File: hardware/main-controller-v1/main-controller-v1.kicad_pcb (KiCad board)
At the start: 2 copper layers, 213.5 x 134.1 mm, 63 parts, among them J1 USB_C_Receptacle_USB2.0_16P, J2 Screw_Terminal_01x02, J3 Screw_Terminal_01x02, J4 Screw_Terminal_01x02, J6 Screw_Terminal_01x14, K1 G3MB-202P, K10 G3MB-202P, K11 G3MB-202P, K12 G3MB-202P, K2 G3MB-202P, K3 G3MB-202P, K4 G3MB-202P, K5 G3MB-202P, K6 G3MB-202P, K7 G3MB-202P, K8 G3MB-202P, K9 G3MB-202P, SW1 SW_Push, SW2 SW_Push, U1 ESP32-S3-WROOM-1, U2 USBLC6-2SC6, U3 LM2596S-5, U4 AP2112K-3.3

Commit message: feat(hardware): WP-24BF*15 PCB outline with parametric IR + KiCad renderer
Board outline for the smaller Polycase WP-24BF*15 enclosure, driven by a
JSON intermediate representation so future geometry tweaks stay in one place.

- board_ir.json: authoritative dimensions in inches, origin at board center.
  Includes concave R.300 corner scoops (to clear lid-screw bosses),
  case-rib alignment notches, 4 corner mounting holes, and a top-edge
  antenna cutout (20 mm x 8.75 mm) sized to clear the WROOM-1 antenna
  keep-out plus the same boss column that the standard case-rib notches
  address.
- preview_outline.py: matplotlib preview emitting the same segment list
  the KiCad renderer consumes, with a closure check so gaps are caught
  before touching the .pcb.
- draw_24f_outline.py: KiCad 10 Python-console script that reuses the
  preview's outline walker, converts inches->mm with a Y-flip, and
  groups everything as "Board Outline 24F".
- .gitignore: ignore KiCad *.kicad_prl (per-user project session state).
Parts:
- removed REF** (x4): MountingHole_3.5mm, MountingHole:MountingHole_3.5mm
- moved K1 161.7 mm to (341.0, 129.9)
- moved K10 161.7 mm to (341.0, 66.7)
- moved K11 161.7 mm to (341.0, 59.9)
- moved K12 161.7 mm to (341.0, 52.9)
- moved K2 161.7 mm to (341.0, 122.9)
- moved K3 161.7 mm to (341.0, 116.1)
- moved K4 161.7 mm to (341.0, 109.0)
- moved K5 161.7 mm to (341.0, 102.0)
- moved K6 161.7 mm to (341.0, 94.9)
- moved K7 161.7 mm to (341.0, 87.9)
- moved K8 161.7 mm to (341.0, 80.9)
- moved K9 161.7 mm to (341.0, 73.9)
- moved R10 161.7 mm to (317.0, 109.2)
- moved R11 161.7 mm to (317.0, 101.7)
- moved R12 161.7 mm to (317.0, 94.7)
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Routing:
- net +5V: track 262.1 -> 0.00 mm, vias 4 -> 0
- net 24VAC_HOT: track 199.3 -> 0.00 mm
- net 24VAC_COM: track 194.5 -> 0.00 mm
- net +3V3: track 148.1 -> 0.00 mm, vias 2 -> 0
- net /ZONE3: track 117.9 -> 0.00 mm, vias 2 -> 0
- net /ZONE1: track 117.9 -> 0.00 mm, vias 2 -> 0
- net /ZONE2: track 109.3 -> 0.00 mm, vias 2 -> 0
- net Net-(U3-GND): track 83.5 -> 0.00 mm, vias 2 -> 0
- net /ZONE5: track 82.8 -> 0.00 mm, vias 2 -> 0
- net /ZONE4: track 81.0 -> 0.00 mm, vias 2 -> 0
- net /LED_DATA: track 74.8 -> 0.00 mm, vias 2 -> 0
- net /RAIN: track 70.5 -> 0.00 mm, vias 2 -> 0
- net /FLOW: track 69.0 -> 0.00 mm, vias 4 -> 0
- net Net-(D3-K): track 67.6 -> 0.00 mm
- net /ZONE6: track 65.5 -> 0.00 mm, vias 2 -> 0
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- removed copper zone on B.Cu, net GND
- removed copper zone on F.Cu, net GND
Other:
- board size 213.5 x 134.1 mm -> 163 x 113 mm

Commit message: feat(hardware): main-controller-v1 routed with GND pours, stitching, and clean DRC
Placed components, routed signal/power nets, added F.Cu + B.Cu GND pours
with edge-clearance auto-clip, stitching vias around U1/U3/USB and along
the perimeter. DRC clean: 0 violations, 0 unconnected items.
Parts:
- added U1: ESP32-S3-WROOM-1, PCM_Espressif:ESP32-S3-WROOM-1, F.Cu at (100.8, -122.7)
- moved K1 173.7 mm to (188.3, 47.0), turned to 180 degrees
- moved K12 168.4 mm to (188.3, 124.0), turned to 180 degrees
- moved R7 168.2 mm to (179.5, 33.3)
- moved K2 167.5 mm to (188.3, 54.0), turned to 180 degrees
- moved K11 163.0 mm to (188.3, 117.0), turned to 180 degrees
- moved K3 162.3 mm to (188.3, 60.9), turned to 180 degrees
- moved R8 161.9 mm to (182.3, 33.3)
- moved K10 158.7 mm to (188.3, 110.2), turned to 180 degrees
- moved K4 158.1 mm to (188.3, 67.9), turned to 180 degrees
- moved R9 155.8 mm to (185.1, 33.3)
- moved K9 155.4 mm to (188.3, 103.0), turned to 180 degrees
- moved K5 155.0 mm to (188.3, 75.0), turned to 180 degrees
- moved K8 153.4 mm to (188.3, 96.0), turned to 180 degrees
- moved K6 153.2 mm to (188.3, 82.0), turned to 180 degrees
- moved K7 152.7 mm to (188.3, 89.0), turned to 180 degrees
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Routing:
- net +5V: track 0.00 -> 196.3 mm, vias 0 -> 4
- net 24VAC_HOT: track 0.00 -> 180.9 mm, vias 0 -> 2
- net /ZONE11: track 0.00 -> 134.7 mm, vias 0 -> 4
- net /ZONE10: track 0.00 -> 125.6 mm, vias 0 -> 2
- net /ZONE12: track 0.00 -> 115.0 mm, vias 0 -> 4
- net /ZONE6: track 0.00 -> 112.8 mm, vias 0 -> 4
- net /ZONE1: track 0.00 -> 112.7 mm, vias 0 -> 4
- net /ZONE8: track 0.00 -> 108.2 mm, vias 0 -> 4
- net /ZONE5: track 0.00 -> 107.1 mm, vias 0 -> 2
- net 24VAC_COM: track 0.00 -> 105.6 mm
- net /ZONE9: track 0.00 -> 104.9 mm, vias 0 -> 2
- net /ZONE4: track 0.00 -> 102.3 mm, vias 0 -> 2
- net Net-(K12-T1): track 0.00 -> 101.2 mm
- net /ZONE7: track 0.00 -> 100.5 mm, vias 0 -> 2
- net /ZONE3: track 0.00 -> 98.0 mm, vias 0 -> 2
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- added copper zone on B.Cu, net GND
- added copper zone on F.Cu, net GND
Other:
- board size 163 x 113 mm -> 162.7 x 112.7 mm

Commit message: fix(hardware): correct U3 GND, add fiducials, fix +VRAW via geometry
- Replace U3 pin 3 PWR_FLAG with GND power symbol; buck now has proper
  GND return through the pour instead of floating on Net-(U3-GND)
- Update PCB from schematic to propagate net changes (K1-K12 coil pins,
  U3 tab pad)
- Route +VRAW at Power netclass, complete U3 OUT -> D3-K -> L1-1
  switch node
- Add 3 fiducials (Fiducial_1mm_Mask3mm, Level A) at TR/BL/BR corners
  for PCBA optical alignment; asymmetric layout for orientation
- Fix +VRAW vias: swap diameter/hole (were 0.4/0.8, corrected to 0.8/0.4)
- DRC clean: 0 errors, 0 warnings, 0 unconnected items
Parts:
- removed the U1 at (100.8, -122.7)
- added FID1: Fiducial_1mm_Mask3mm, Fiducial:Fiducial_1mm_Mask3mm, F.Cu at (82.5, 133.5)
- added FID2: Fiducial_1mm_Mask3mm, Fiducial:Fiducial_1mm_Mask3mm, F.Cu at (216.5, 133.0)
- added FID3: Fiducial_1mm_Mask3mm, Fiducial:Fiducial_1mm_Mask3mm, F.Cu at (164.0, 41.0)
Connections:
- C6 pad 2: Net-(U3-GND) -> GND
- U3 pad 3: Net-(U3-GND) -> GND
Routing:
- net Net-(U3-GND): track 45.1 -> 0.00 mm
- net 24VAC_HOT: track 180.9 -> 183.8 mm, vias 2 -> 0
- net Net-(D3-K): track 42.5 -> 45.0 mm, vias 0 -> 1
- net /+VRAW: track 48.0 -> 50.0 mm
- net 24VAC_COM: track 105.6 -> 106.7 mm

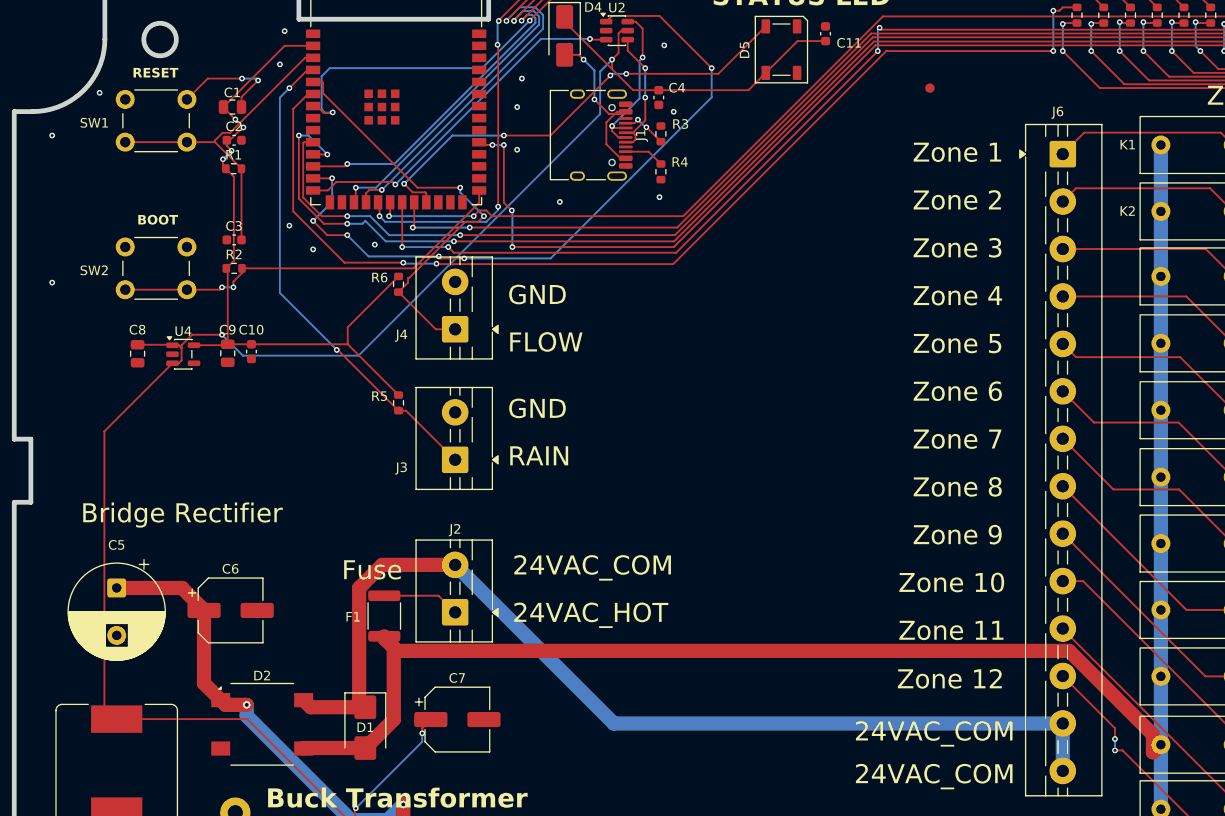
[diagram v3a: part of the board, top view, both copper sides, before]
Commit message: fix(hardware): widen +5V and +3V3 power-rail trunks
Route +5V from L1 output to U4 (LDO input) at 1.5 mm Power netclass width
to handle WiFi TX transient current on the pre-regulator side. Route +3V3
trunk from U4 output up to WROOM VDD3P3 at 0.8 mm — enough for ~100 mA
average with C1 (10 uF) providing local bulk for TX bursts.

Also assign +VRAW and +3V3 to Power netclass in Board Setup so future
routing picks up the correct widths.

Trace-width audit results:
- 24VAC_HOT / 24VAC_COM / +VRAW: 1.5 mm end-to-end (unchanged)
- +5V: 1.5 mm on L1 -> LDO backbone; USB-C VBUS and WS2812B branches
  stay thin (500 mA / 60 mA don't warrant widening)
- +3V3: 0.8 mm on trunk to WROOM; pull-up stubs stay thin
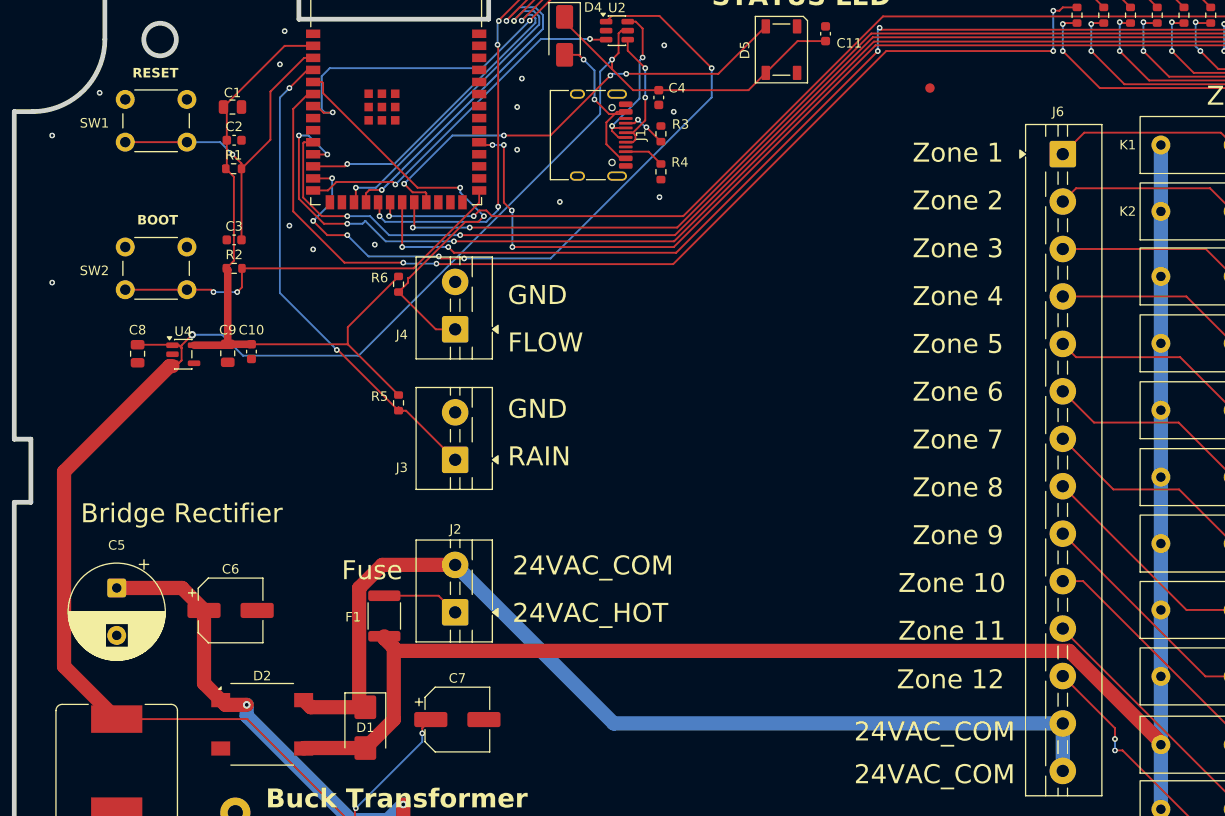
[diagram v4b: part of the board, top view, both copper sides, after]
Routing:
- net GND: track 12.0 -> 0.00 mm, vias 33 -> 31
- net +5V: track 196.3 -> 201.5 mm
- net 24VAC_HOT: track 183.8 -> 182.2 mm
- net Net-(U1-EN): track 35.0 -> 36.6 mm, vias 0 -> 1
- net +3V3: track 73.6 -> 72.4 mm, vias 4 -> 0
- net Net-(U1-GPIO0/BOOT): track 43.0 -> 43.8 mm

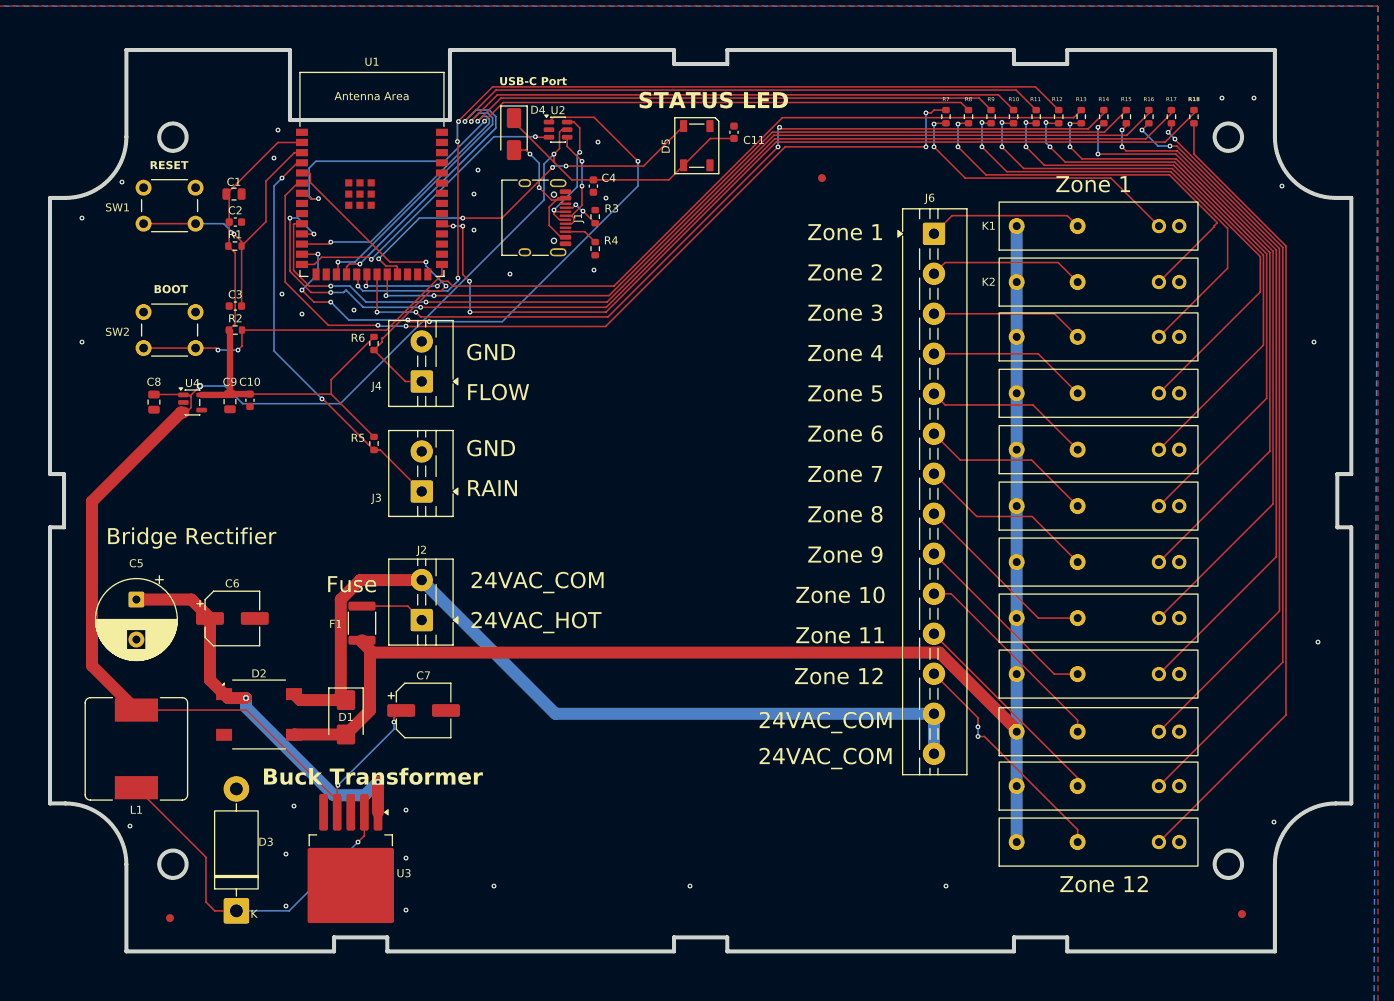
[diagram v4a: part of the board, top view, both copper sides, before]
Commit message: chore(hardware): rev1 fab snapshot + rev2 workspace scaffolding
Rev1 fab archive relocated + canonical:
- Move gerbers to hardware/main-controller-v1/production/gerbers/ with
  proper KiCad per-layer extensions (.gtl/.gbl/.gts/.gbs/.gto/.gbo/.gm1
  /.gtp/.gbp) and drop legacy flat-.gbr copies.
- Add production/main-controller-v1-gerbers.zip and CSV BOM/CPL —
  the shipped-to-JLC package.
- Mark scripts/preview_gerbers/ as ephemeral (paper-template only,
  do not upload to fab; enforced via .gitignore).

Rev2 workspace scaffolding:
- parts.yaml: BOM source of truth grouped by (value, footprint), with
  fate: smt/dnp and LCSC assignments.
- fabrication-toolkit-options.json: Fabrication Toolkit config.
- scripts/apply_lcsc_fields.py: apply parts.yaml → schematic LCSC fields.
- scripts/export_jlc_package.sh: one-shot fab-package export with
  CP_Elec/SOT-23/SOIC/QFP rotation offsets baked in.
- scripts/enclosure_drill_template.{pdf,svg}: enclosure hole/notch
  drilling template.
- scripts/wiring_form_template.{pdf,svg}: field-install wiring form.

PCB + supporting file updates:
- kicad_pcb: solder-mask/track-width tweaks + routing progress.
- kicad_pro: DRC + track width table, ERC exclusion for D2 lib mismatch,
  designator refresh.
- Azul.pretty/G3MB-202P.kicad_mod: SSR footprint touch-up.
- scripts/preview_outline.py + draw_24f_outline.py + board_ir.json +
  board_preview.png: outline renderer parity with corner-fillet spec.
- docs/design/main-controller-pcb-v1.md: design doc refresh.

Correspondence + status artifacts (JLC / Picker / order tracking):
- JLC_D2_PINOUT_HALT.md, JLC_ORDER_CANCEL_REQUEST.md,
  JLC_SUPPORT_MESSAGE.md, JLC_SUPPORT_REPLY.md,
  JLC_SUPPORT_REPLY_G3MB.md, JLC_SUPPORT_STATUS_CHECK.md,
  JLC_WROOM_2D_VIEW_REQUEST.md, PICKER_SSR_REPLY.md,
  ORDER_STATUS.md, enclosure_hole_plan.md,
  gerbers/main-controller-v1.pdf (schematic PDF export),
  PCB Image from JLCPCB.png.
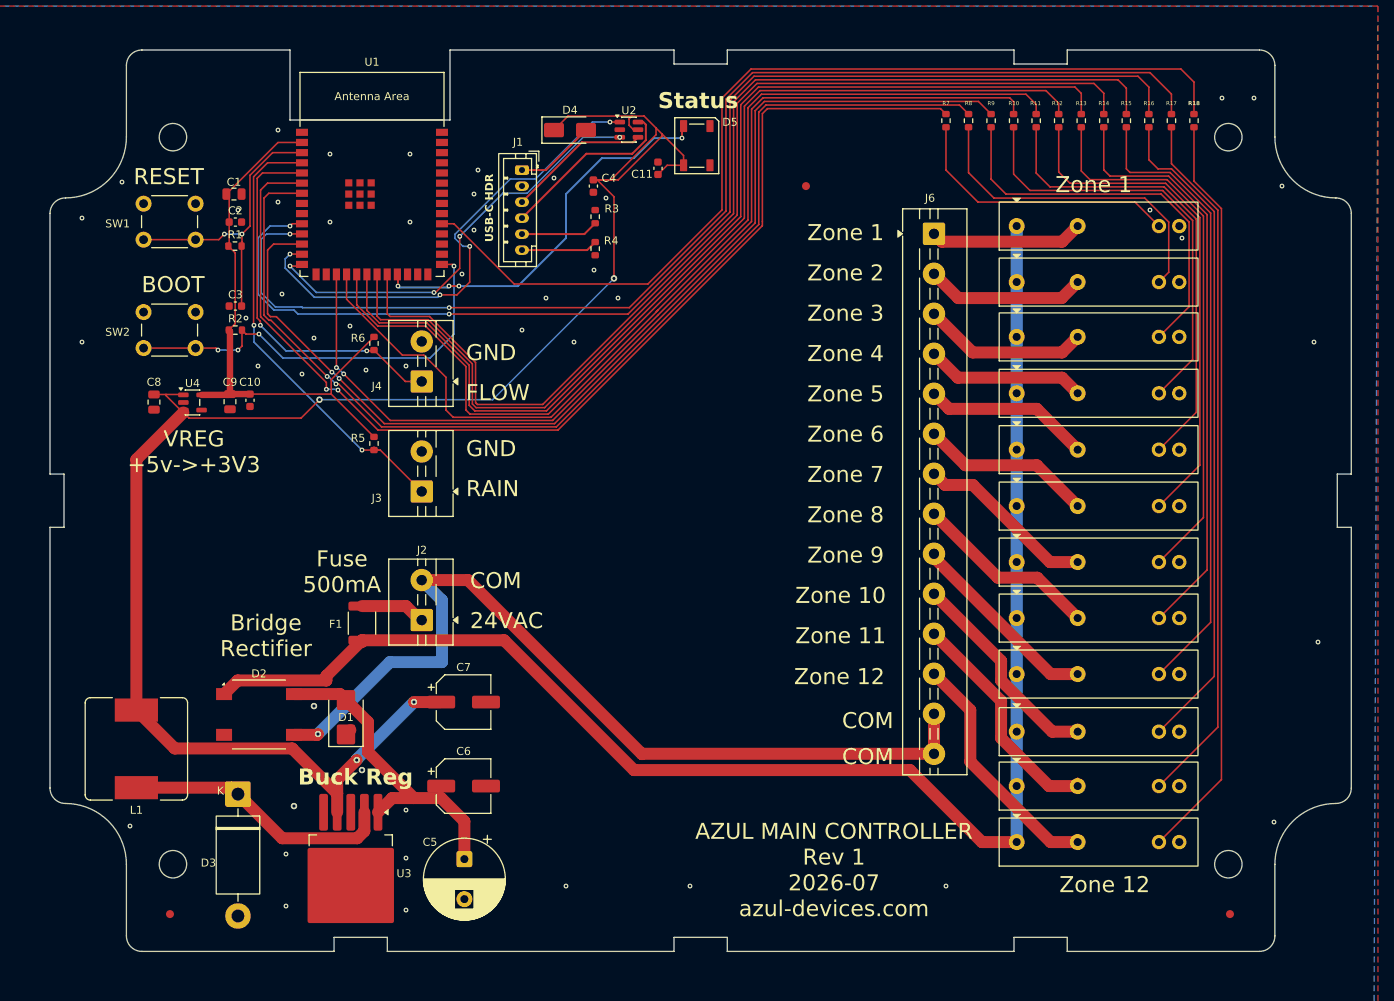
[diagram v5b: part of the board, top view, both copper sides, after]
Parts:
- FID1, FID2, FID3: value Fiducial_1mm_Mask3mm -> Fiducial; footprint Fiducial:Fiducial_1mm_Mask3mm -> Fiducial:Fiducial_1mm_Mask2mm
- J1: value USB_C_Receptacle_USB2.0_16P -> B6B-PH-K-S; footprint Connector_USB:USB_C_Receptacle_HRO_TYPE-C-31-M-12 -> Connector_JST:JST_PH_B6B-PH-K_1x06_P2.00mm_Vertical
- moved C5 52.3 mm to (119.3, 126.1)
- moved C6 35.7 mm to (119.2, 117.0)
- moved D3 14.6 mm to (91.0, 118.0), turned to -90 degrees
- moved C11 10.5 mm to (143.5, 39.8)
- moved U2 8.85 mm to (139.9, 35.0)
- moved D4 7.02 mm to (132.5, 35.0), turned to 0 degrees
- moved J1 6.12 mm to (126.5, 40.0)
- moved C7 5.11 mm to (119.2, 106.5)
- moved FID3 2.24 mm to (162.0, 42.0)
- moved SW1 2.00 mm to (79.2, 44.2)
- moved FID2 1.50 mm to (215.0, 133.0)
- moved FID1 0.50 mm to (82.5, 133.0)
- moved R10 0.50 mm to (188.0, 33.8)
- moved R11 0.50 mm to (190.8, 33.8)
- moved R12 0.50 mm to (193.6, 33.8)
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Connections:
- D1 pad 1: 24VAC_COM -> GND
- D1 pad 2: 24VAC_HOT -> /+VRAW
- D2 pad 1: /+VRAW -> 24VAC_HOT
- D2 pad 3: 24VAC_HOT -> 24VAC_COM
- D2 pad 4: 24VAC_COM -> /+VRAW
- R3 pad 1: Net-(J1-CC1) -> Net-(J1-Pin_5)
- R4 pad 1: Net-(J1-CC2) -> Net-(J1-Pin_6)
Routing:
- net /ZONE2: track 93.4 -> 138.8 mm
- net /ZONE3: track 98.0 -> 134.3 mm
- net /ZONE7: track 100.5 -> 129.8 mm, vias 2 -> 0
- net /ZONE9: track 104.9 -> 133.6 mm, vias 2 -> 0
- net /ZONE1: track 112.7 -> 139.1 mm, vias 4 -> 2
- net /ZONE10: track 125.6 -> 150.1 mm
- net /ZONE8: track 108.2 -> 131.8 mm, vias 4 -> 0
- net /ZONE4: track 102.3 -> 125.7 mm
- net +5V: track 201.5 -> 221.0 mm
- net /ZONE5: track 107.1 -> 124.8 mm, vias 2 -> 0
- net /USB_D+: track 37.7 -> 55.2 mm, vias 2 -> 4
- net /ZONE11: track 134.7 -> 150.6 mm, vias 4 -> 2
- net /ZONE6: track 112.8 -> 127.3 mm, vias 4 -> 0
- net /USB_D-: track 74.7 -> 62.5 mm, vias 6 -> 4
- net Net-(D3-K): track 45.0 -> 33.8 mm, vias 1 -> 0
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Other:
- outline, holes or cut-outs redrawn
- board text added: "24VAC"
- board text added: "AZUL MAIN CONTROLLER Rev 1 2026-07 azul-devices.com"
- board text added: "Buck Reg"
- board text added: "COM"
- board text added: "Fuse 500mA"
- board text added: "Status"
- board text added: "USB-C HDR"
- board text added: "VREG +5v->+3V3"
- board text removed: "24VAC_COM"
- board text removed: "24VAC_HOT"
- board text removed: "Buck Transformer"
- board text removed: "Fuse"
- board text removed: "STATUS LED"
- board text removed: "USB-C Port"
